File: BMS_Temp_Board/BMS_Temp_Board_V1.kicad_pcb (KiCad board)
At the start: 4 copper layers, 190.5 x 74.1 mm, 77 parts, among them IC1 ESP32-S3-WROOM-1-N8R8, IC10 CD74HC4067PWR, IC11 CD74HC4067PWR, IC12 CD74HC4067PWR, IC13 CD74HC4067PWR, IC14 CD74HC4067PWR, IC15 CD74HC4067PWR, IC2 CP2102N-A02-GQFN28, IC3 TLP175A_TPL,E, IC4 TPS2116DRLR, IC5 MIC37100-3.3WS, IC6 CD74HC4067PWR, IC7 CD74HC4067PWR, IC8 CD74HC4067PWR, IC9 CD74HC4067PWR, J1 ESP_USB, J10 B32B-PUDSS-1_LF__SN_, J11 B32B-PUDSS-1_LF__SN_, J12 B2B-PH-K-S, J13 SM04B-ULHK-1TA1-ETB_HF_, J14 B2B-PH-K-S, J2 B32B-PUDSS-1_LF__SN_, J3 B32B-PUDSS-1_LF__SN_, J4 B32B-PUDSS-1_LF__SN_, J5 B32B-PUDSS-1_LF__SN_, J6 B32B-PUDSS-1_LF__SN_, J7 B32B-PUDSS-1_LF__SN_, J8 B32B-PUDSS-1_LF__SN_, J9 B32B-PUDSS-1_LF__SN_, Q1 MMBT2222LT1G, Q2 MMBT2222LT1G, U1 USBLC6-2SC6, U2 SN65HVD230, U3 LM2575HVS-5.0_NOPB

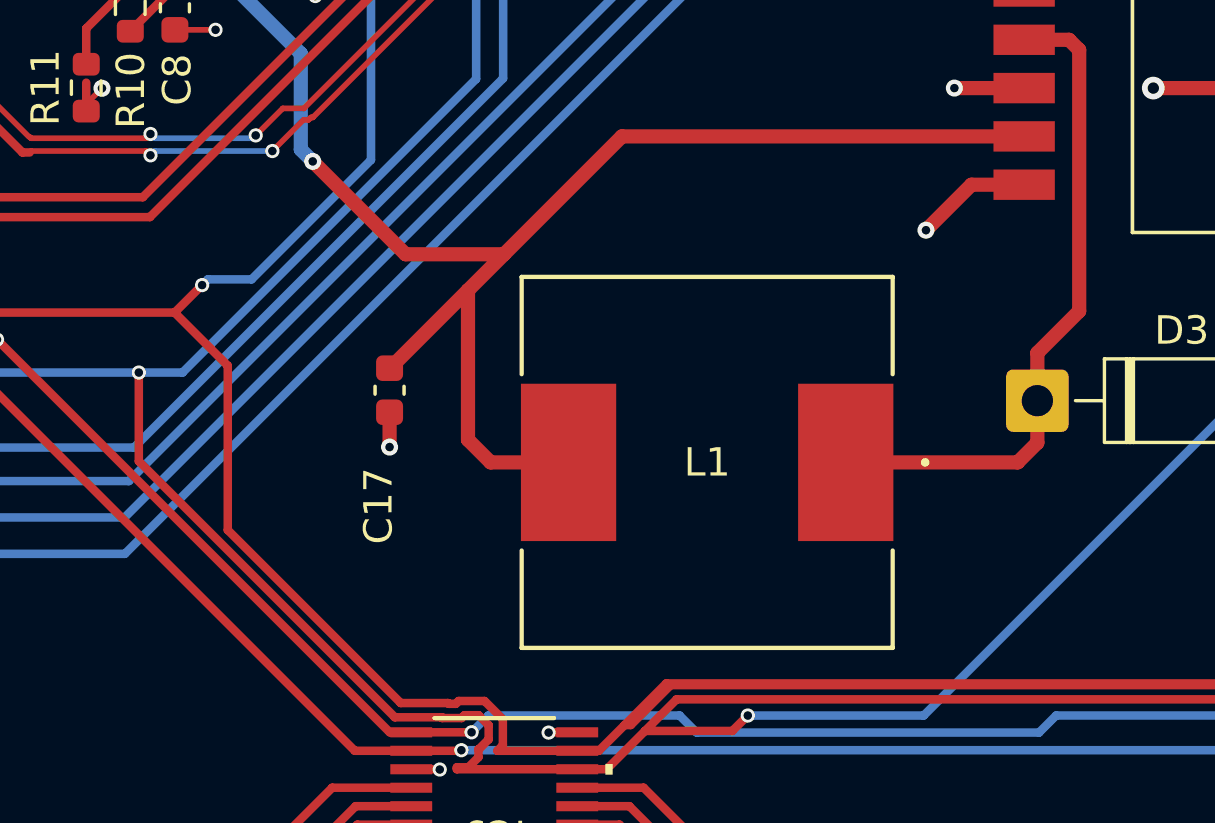
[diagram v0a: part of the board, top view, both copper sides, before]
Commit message: changed C17 and some layout on bms temp
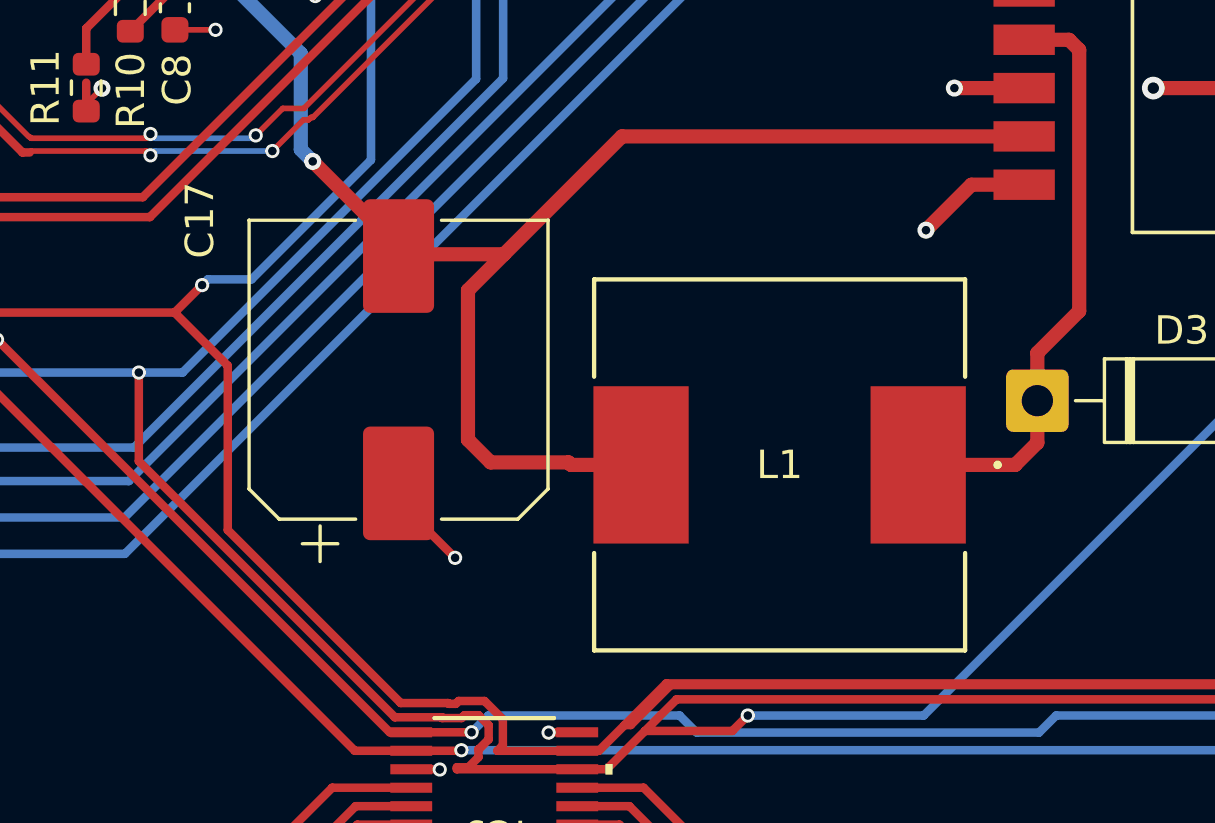
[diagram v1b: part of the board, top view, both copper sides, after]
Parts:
- C17: footprint Capacitor_SMD:C_0603_1608Metric -> Capacitor_SMD:CP_Elec_10x10
- moved L1 2.55 mm to (116.8, 106.3)
- moved C17 0.79 mm to (103.4, 102.9)
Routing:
- net Net-(D3-K): track 23.5 -> 21.0 mm
- net GND: track 116.5 -> 118.7 mm
- net VCC: track 65.1 -> 63.8 mm

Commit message: made changes from design review
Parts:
- removed J13: SM04B-ULHK-1TA1-ETB_HF_, SM04B-ULH:SM04BULHK1TA1ETBHF
- added J15: B2B-PH-K-S, B2B_PH_K_S:JST_B2B-PH-K-S, F.Cu at (85.8, 94.0)
- added R17: 10k, Resistor_SMD:R_0603_1608Metric, F.Cu at (196.7, 122.7)
- added R18: 10k, Resistor_SMD:R_0603_1608Metric, F.Cu at (160.8, 122.2)
- added R19: 10k, Resistor_SMD:R_0603_1608Metric, F.Cu at (124.7, 121.7)
- added R20: 10k, Resistor_SMD:R_0603_1608Metric, F.Cu at (88.9, 120.3)
- added R21: 10k, Resistor_SMD:R_0603_1608Metric, F.Cu at (74.8, 113.8)
- added R22: 10k, Resistor_SMD:R_0603_1608Metric, F.Cu at (197.3, 77.3)
- added R23: 10k, Resistor_SMD:R_0603_1608Metric, F.Cu at (161.3, 77.3)
- added R24: 10k, Resistor_SMD:R_0603_1608Metric, F.Cu at (125.2, 77.0)
- added R25: 10k, Resistor_SMD:R_0603_1608Metric, F.Cu at (108.8, 89.2)
- added R26: 10k, Resistor_SMD:R_0603_1608Metric, F.Cu at (75.3, 104.5)
- C15: footprint Capacitor_SMD:C_0603_1608Metric -> 865080545012:WCAP-ASLI_6.3X7.7_DXL_
- D3: value 1N5819 -> SS14; footprint Diode_THT:D_DO-41_SOD81_P10.16mm_Horizontal -> Diode_SMD:D_SMA
- moved C15 9.23 mm to (118.8, 86.0), turned to 0 degrees
- moved D3 2.21 mm to (128.1, 104.0)
- moved LED1 1.09 mm to (61.7, 116.7)
- moved R2 0.83 mm to (64.7, 116.6)
- moved C17 0.50 mm to (103.3, 102.4), turned to -90 degrees
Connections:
- C15 pad 1: GND -> +12V
- C15 pad 2: +12V -> GND
- C17 pad 1: GND -> VCC
- C17 pad 2: VCC -> GND
- IC1 pad 10: unconnected-(IC1-IO17-Pad10) -> /MUX5
- IC1 pad 16: /MUX5 -> unconnected-(IC1-IO46-Pad16)
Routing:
- net /CAN+: track 220.9 -> 10.4 mm, vias 2 -> 0
- net /CAN-: track 221.8 -> 22.7 mm, vias 4 -> 2
- net +5V: track 161.1 -> 20.6 mm, vias 2 -> 0
- net /MUX5: track 15.3 -> 30.7 mm, vias 0 -> 4
- net GND: track 118.7 -> 130.4 mm, vias 57 -> 66
- net /MUX10: track 33.1 -> 38.6 mm, vias 2 -> 4
- net Net-(IC11-I0): track 15.8 -> 19.9 mm
- net Net-(IC11-I15): track 16.2 -> 20.0 mm
- net /MUX1: track 159.0 -> 162.5 mm, vias 2 -> 3
- net Net-(IC11-I14): track 14.0 -> 17.3 mm
- net +12V: track 9.12 -> 12.5 mm
- net Net-(IC12-I15): track 16.2 -> 19.4 mm
- net Net-(IC11-I1): track 14.0 -> 17.2 mm
- net Net-(IC12-I0): track 15.8 -> 18.9 mm
- net Net-(IC12-I14): track 14.0 -> 16.8 mm
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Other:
- board text added: "-"
- board text added: "CAN+"

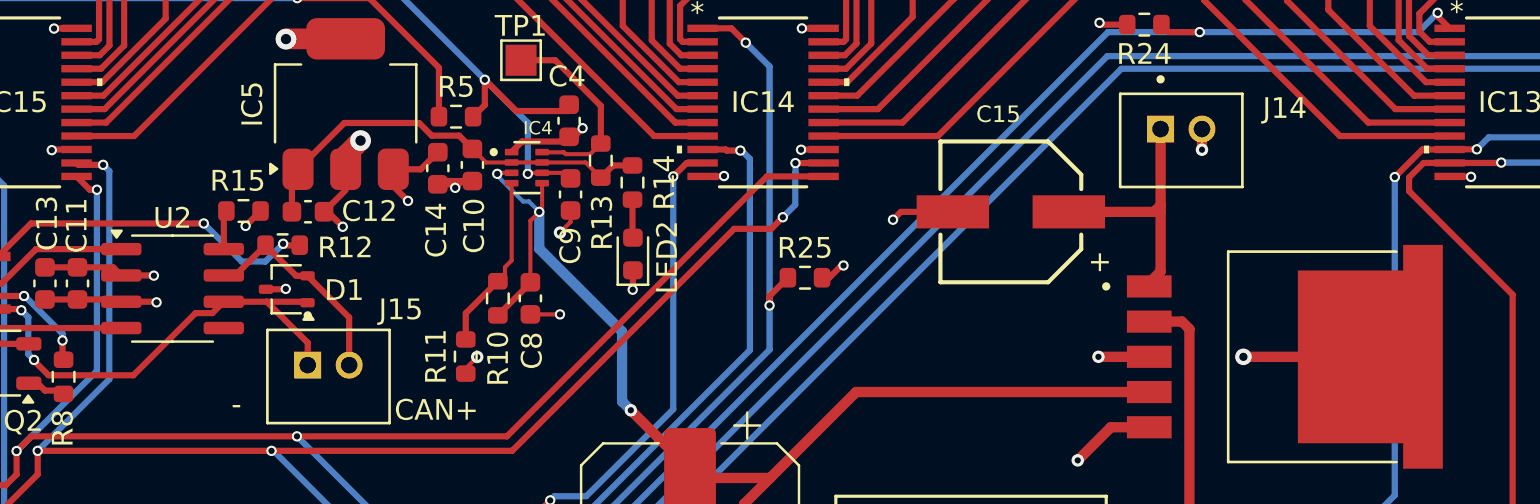
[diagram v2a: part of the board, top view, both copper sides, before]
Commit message: changed capacitor footprint, prolly something else too
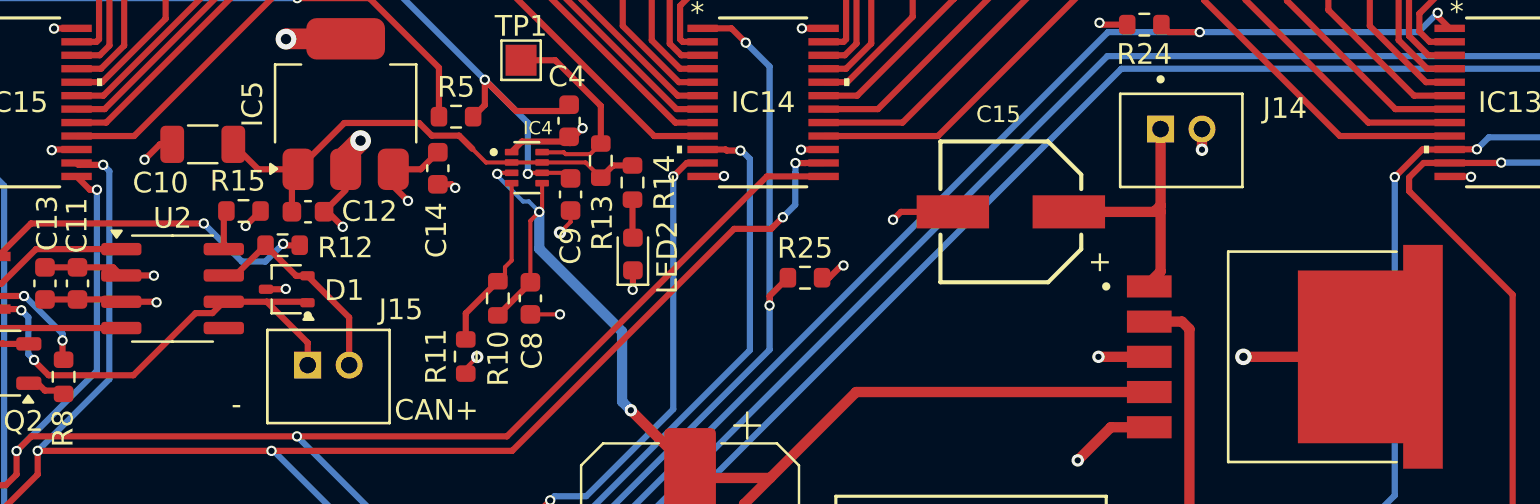
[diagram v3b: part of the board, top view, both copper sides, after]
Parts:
- C10: footprint Capacitor_SMD:C_0603_1608Metric -> Capacitor_SMD:C_1206_3216Metric
- moved C10 13.1 mm to (79.8, 82.7), turned to 180 degrees
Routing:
- net GND: track 130.4 -> 122.8 mm, vias 66 -> 67
- net +5V: track 20.6 -> 24.2 mm
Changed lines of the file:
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@@
 		)
 	)
-	(footprint "Capacitor_SMD:C_0603_1608Metric"
+	(footprint "Capacitor_SMD:C_1206_3216Metric"
 		(layer "F.Cu")
-		(at 92.771 83.734999 -90)
-		(descr "Capacitor SMD 0603 (1608 Metric), square (rectangular) end terminal, IPC-7351 nominal, (Body size source: IPC-SM-782 page 76, https://www.pcb-3d.com/wordpress/wp-content/uploads/ipc-sm-782a_amendment_1_and_2.pdf), generated with kicad-footprint-generator")
+		(at 79.75 82.74 180)
+		(descr "Capacitor SMD 1206 (3216 Metric), square (rectangular) end terminal, IPC-7351 nominal, (Body size source: IPC-SM-782 page 76, https://www.pcb-3d.com/wordpress/wp-content/uploads/ipc-sm-782a_amendment_1_and_2.pdf), generated with kicad-footprint-generator")
 		(tags "capacitor")
 		(property "Reference" "C10"
-			(at 2.94 -0.09 90)
+			(at 2.04 -1.86 0)
 			(layer "F.SilkS")
 			(effects
@@
 		)
 		(property "Value" "100uF"
-			(at 0 1.43 90)
+			(at 0 1.85 0)
 			(layer "F.Fab")
 			(effects
@@
 		)
 		(property "Datasheet" "~"
-			(at 0 0 90)
+			(at 0 0 0)
 			(layer "F.Fab")
 			(hide yes)
@@
 		)
 		(property "Description" ""
-			(at 0 0 90)
+			(at 0 0 0)
 			(layer "F.Fab")
 			(hide yes)
@@
 		(attr smd)
 		(fp_line
-			(start -0.14058 0.51)
-			(end 0.14058 0.51)
+			(start -0.711252 0.91)
+			(end 0.711252 0.91)
 			(stroke
 				(width 0.12)
@@
 		)
 		(fp_line
-			(start -0.14058 -0.51)
-			(end 0.14058 -0.51)
+			(start -0.711252 -0.91)
+			(end 0.711252 -0.91)
 			(stroke
 				(width 0.12)
@@
 		)
 		(fp_line
-			(start -1.48 0.73)
-			(end -1.48 -0.73)
+			(start 2.3 1.15)
+			(end -2.3 1.15)
 			(stroke
 				(width 0.05)
@@
 		)
 		(fp_line
-			(start 1.48 0.73)
-			(end -1.48 0.73)
+			(start 2.3 -1.15)
+			(end 2.3 1.15)
 			(stroke
 				(width 0.05)
@@
 		)
 		(fp_line
-			(start -1.48 -0.73)
-			(end 1.48 -0.73)
+			(start -2.3 1.15)
+			(end -2.3 -1.15)
 			(stroke
 				(width 0.05)
@@
 		)
 		(fp_line
-			(start 1.48 -0.73)
-			(end 1.48 0.73)
+			(start -2.3 -1.15)
+			(end 2.3 -1.15)
 			(stroke
 				(width 0.05)
@@
 		)
 		(fp_line
-			(start -0.8 0.4)
-			(end -0.8 -0.4)
+			(start 1.6 0.8)
+			(end -1.6 0.8)
 			(stroke
 				(width 0.1)
@@
 		)
 		(fp_line
-			(start 0.8 0.4)
-			(end -0.8 0.4)
+			(start 1.6 -0.8)
+			(end 1.6 0.8)
 			(stroke
 				(width 0.1)
@@
 		)
 		(fp_line
-			(start -0.8 -0.4)
-			(end 0.8 -0.4)
+			(start -1.6 0.8)
+			(end -1.6 -0.8)
 			(stroke
 				(width 0.1)
@@
 		)
 		(fp_line
-			(start 0.8 -0.4)
-			(end 0.8 0.4)
+			(start -1.6 -0.8)
+			(end 1.6 -0.8)
 			(stroke
 				(width 0.1)
@@
 		)
 		(fp_text user "${REFERENCE}"
-			(at 0 0 90)
+			(at 0 0 0)
 			(layer "F.Fab")
 			(effects
 				(font
-					(size 0.4 0.4)
-					(thickness 0.06)
+					(size 0.8 0.8)
+					(thickness 0.12)
 				)
 			)
 		)
 		(pad "1" smd roundrect
-			(at -0.775 0 270)
-			(size 0.9 0.95)
+			(at -1.475 0 180)
+			(size 1.15 1.8)
 			(layers "F.Cu" "F.Mask" "F.Paste")
-			(roundrect_rratio 0.25)
+			(roundrect_rratio 0.217391)
 			(net 10 "+5V")
 			(pintype "passive")
 		)
 		(pad "2" smd roundrect
-			(at 0.775 0 270)
-			(size 0.9 0.95)
+			(at 1.475 0 180)
+			(size 1.15 1.8)
 			(layers "F.Cu" "F.Mask" "F.Paste")
-			(roundrect_rratio 0.25)
+			(roundrect_rratio 0.217391)
 			(net 5 "GND")
 			(pintype "passive")
 		)
 		(embedded_fonts no)
-		(model "${KICAD9_3DMODEL_DIR}/Capacitor_SMD.3dshapes/C_0603_1608Metric.step"
+		(model "${KICAD9_3DMODEL_DIR}/Capacitor_SMD.3dshapes/C_1206_3216Metric.step"
 			(offset
 				(xyz 0 0 0)
@@
 	)
 	(segment
-		(start 92.771 84.509999)
-		(end 91.261 84.509999)
-		(width 0.3)
-		(layer "F.Cu")
-		(net 5)
-	)
-	(segment
 		(start 97 90.95)
 		(end 95.57 90.95)
@@
 	)
 	(segment
-		(start 92.270001 84.509999)
-		(end 91.94 84.84)
-		(width 0.3)
-		(layer "F.Cu")
-		(net 5)
-	)
-	(segment
 		(start 97.405 82.603999)
 		(end 95.166 82.603999)
@@
 	)
 	(segment
-		(start 138.221 89.779)
-		(end 138.221 89.221)
-		(width 0.2)
-		(layer "F.Cu")
-		(net 5)
-	)
-	(segment
 		(start 110 89.18)
 		(end 110.55 88.63)
@@
 	)
 	(segment
-		(start 134 94)
-		(end 138.221 89.779)
-		(width 0.2)
-		(layer "F.Cu")
-		(net 5)
-	)
-	(segment
 		(start 113.46 86)
 		(end 113.08 86.38)
@@
 	)
 	(segment
-		(start 92.771 84.509999)
-		(end 92.270001 84.509999)
-		(width 0.3)
-		(layer "F.Cu")
-		(net 5)
-	)
-	(segment
 		(start 60.401 105.014999)
 		(end 57.601 105.014999)
@@
 	)
 	(segment
-		(start 91.261 84.509999)
-		(end 91.101 84.669999)
-		(width 0.3)
-		(layer "F.Cu")
-		(net 5)
-	)
-	(segment
 		(start 75.816 89.069999)
 		(end 77.379999 89.069999)
@@
 	)
 	(segment
+		(start 77.68 82.74)
+		(end 76.94 83.48)
+		(width 0.3)
+		(layer "F.Cu")
+		(net 5)
+	)
+	(segment
 		(start 51.281 113.664999)
 		(end 51.281 112.381)
@@
 	)
 	(segment
+		(start 78.275 82.74)
+		(end 77.68 82.74)
+		(width 0.3)
+		(layer "F.Cu")
+		(net 5)
+	)
+	(segment
 		(start 63.876 83.484999)
 		(end 63.876 83.174)
@@
 	)
 	(segment
-		(start 97.51 86.01)
-		(end 97.51 85.935)
-		(width 0.3)
-		(layer "F.Cu")
-		(net 5)
-	)
-	(segment
 		(start 59.001 105.014999)
 		(end 59.001 106.414999)
@@
 	)
 	(via
+		(at 76.94 83.48)
+		(size 0.5)
+		(drill 0.3)
+		(layers "F.Cu" "B.Cu")
+		(net 5)
+	)
+	(via
 		(at 113.08 86.38)
 		(size 0.5)
@@
 	)
 	(segment
+		(start 82.429999 83.944999)
+		(end 84.351 83.944999)
+		(width 0.3)
+		(layer "F.Cu")
+		(net 10)
+	)
+	(segment
 		(start 94.666 83.614999)
 		(end 93.426 83.614999)
@@
 		(layer "F.Cu")
 		(net 10)
+	)
+	(segment
+		(start 81.225 82.74)
+		(end 82.429999 83.944999)
+		(width 0.3)
+		(layer "F.Cu")
+		(net 10)
